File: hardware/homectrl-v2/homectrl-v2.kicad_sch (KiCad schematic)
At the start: 125 parts, among them J1 Barrel_Jack, J2 PUMP1_CONN, J3 PUMP2_CONN, J4 STEP_CONN, J5 USB_C_CONN, J6 SMS1_CONN, J7 ALS_CONN, J8 FSW1_CONN, Q1 AO3407A, Q2 2N7002, Q3 ZXMN3A01ZTA, Q4 ZXMN3A01ZTA, Q5 AO3400A, SW1 S3_RESET_SW, SW2 S3_BOOT_SW, U1 TPS5405DR, U2 MCP1826S, U3 DMP4065S-7, U4 ESP32-S3-WROOM-1, U5 TMC2209, U7 TPD4E001DRLR, U8 TPD2E001DRLR, U9 SI2347DS-T1-GE3

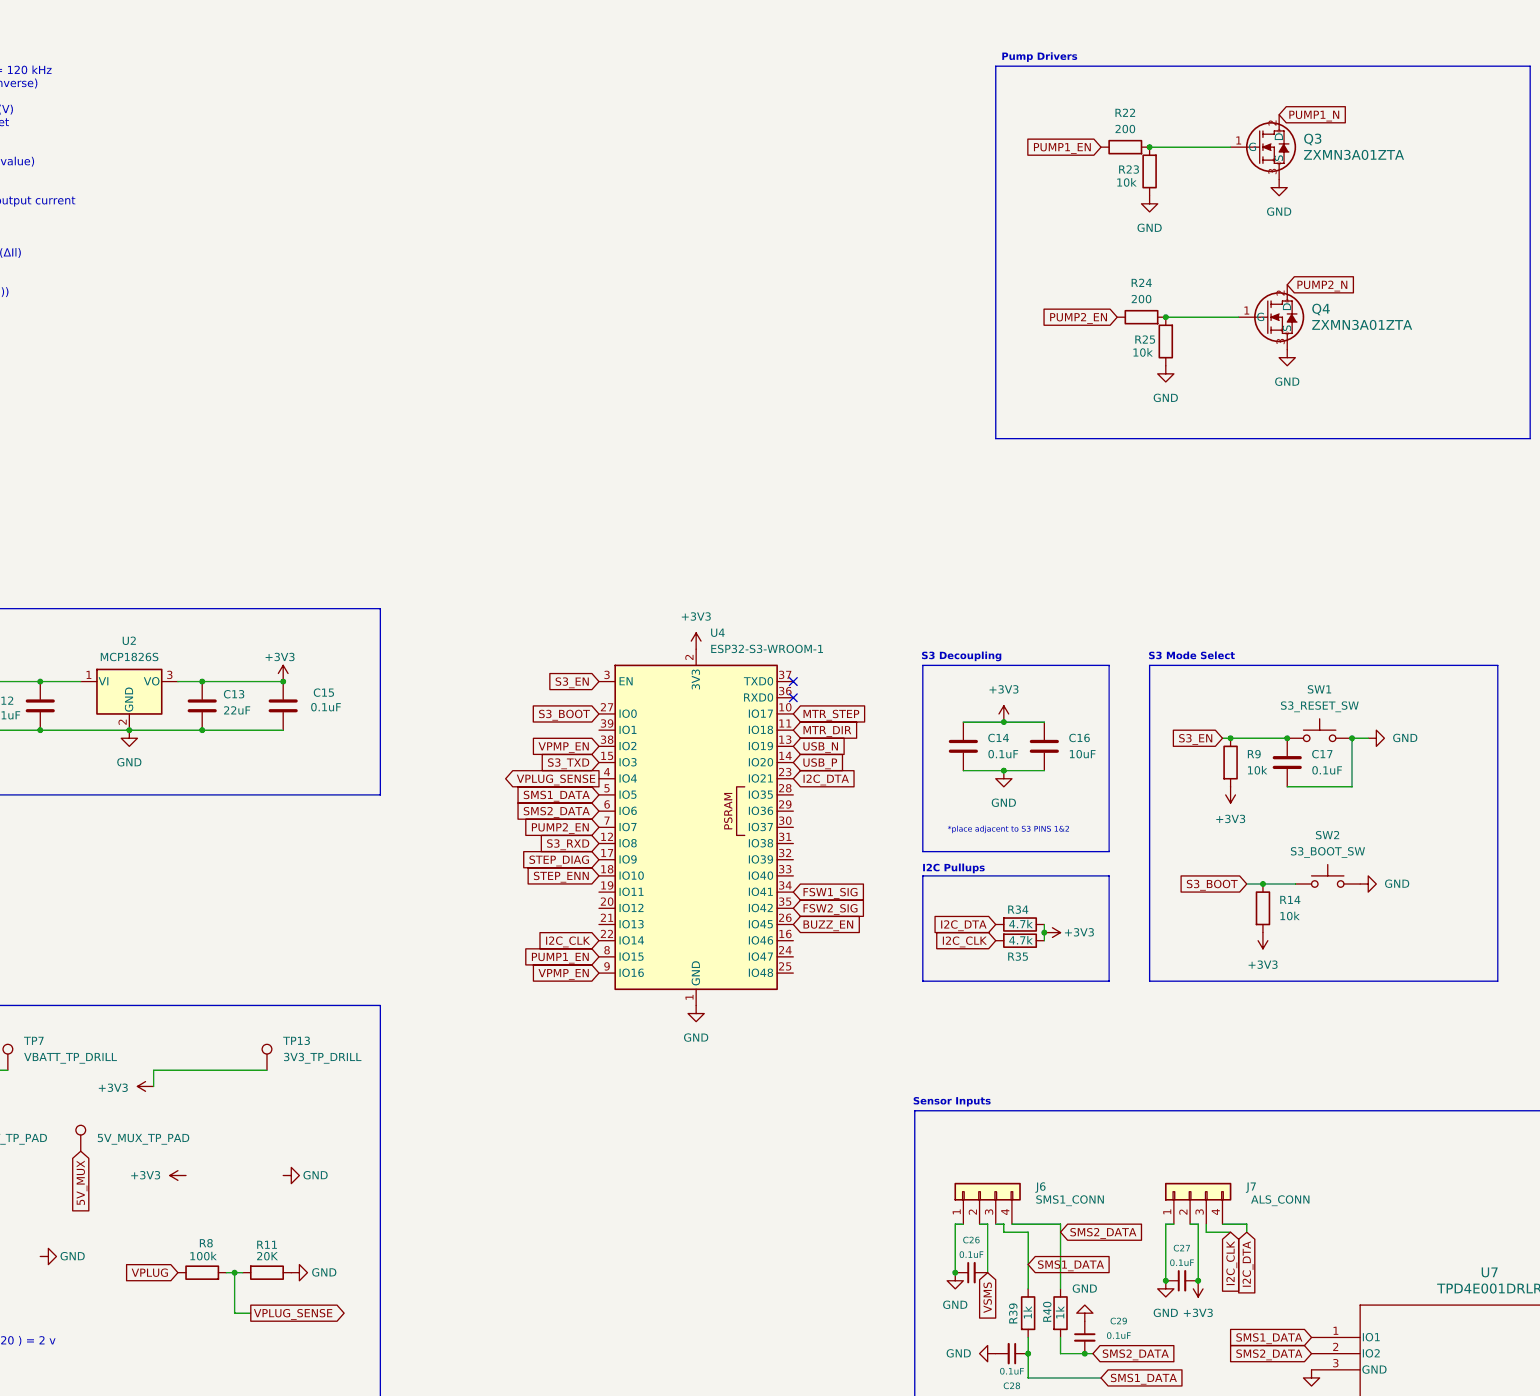
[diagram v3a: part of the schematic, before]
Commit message: finish component routing
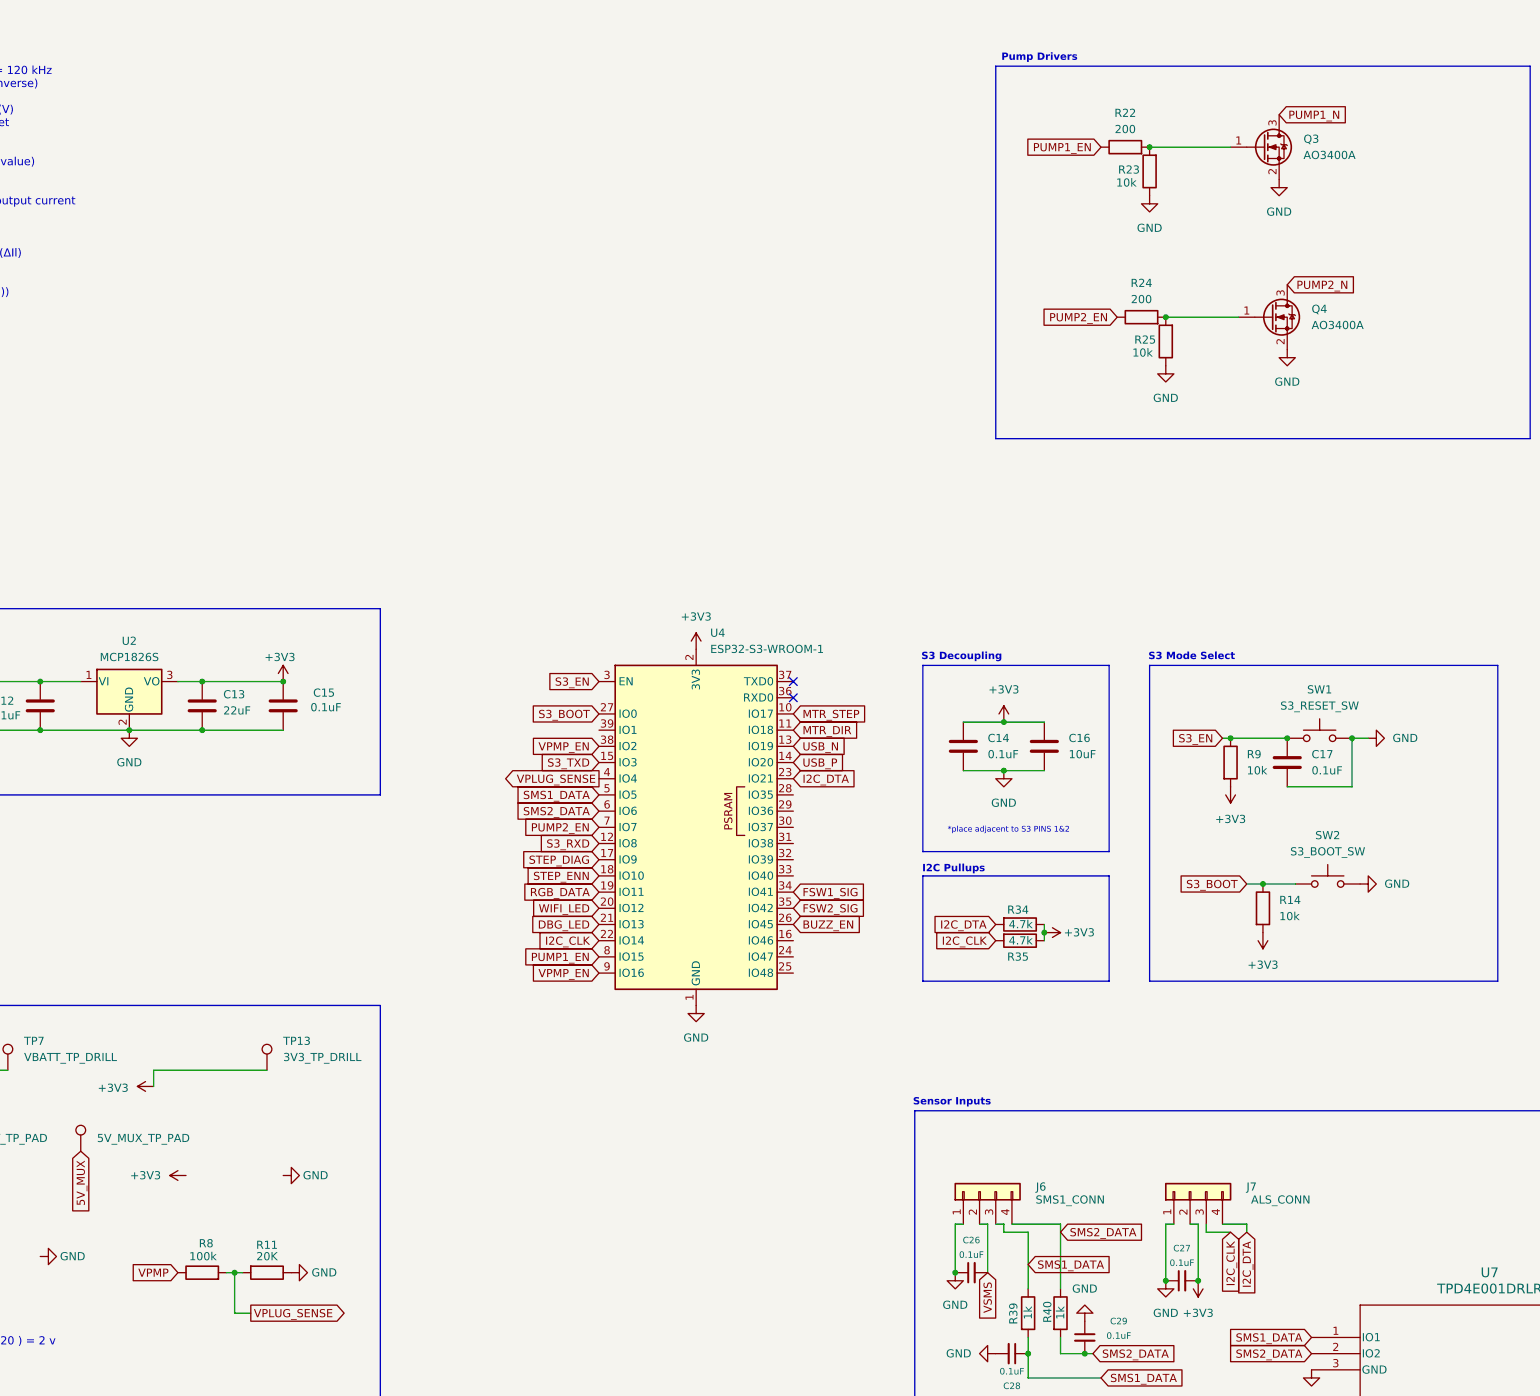
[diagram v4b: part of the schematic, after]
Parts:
- removed Q3, Q4: ZXMN3A01ZTA, Package_TO_SOT_SMD:SOT-89-3, symbol ZXMN3A01ZTA:ZXMN3A01ZTA
- added Q3, Q4: AO3400A, Package_TO_SOT_SMD:SOT-23, symbol Transistor_FET:AO3400A
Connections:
- net DBG_LED: now also U4.21 (IO13)
- net GND: now also Q3.2 (S), Q4.2 (S)
- net PUMP1_N: now also Q3.3 (D)
- net PUMP2_N: now also Q4.3 (D)
- net RGB_DATA: now also U4.19 (IO11)
- net VPLUG: no longer R8.1
- net VPMP: now also R8.1
- net WIFI_LED: now also U4.20 (IO12)
- net at R22.2, R23.2: now also Q3.1 (G)
- net at R24.2, R25.2: now also Q4.1 (G)
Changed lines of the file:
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@@
 		)
 	)
+	(global_label "WIFI_LED"
+		(shape input)
+		(at 259.08 226.06 180)
+		(fields_autoplaced yes)
+		(effects
+			(font
+				(size 1.27 1.27)
+			)
+			(justify right)
+		)
+		(property "Intersheetrefs" "${INTERSHEET_REFS}"
+			(at 247.9305 226.06 0)
+			(effects
+				(font
+					(size 1.27 1.27)
+				)
+				(justify right)
+				(hide yes)
+			)
+		)
+	)
 	(global_label "I2C_CLK"
 		(shape input)
@@
 		)
 	)
+	(global_label "VPMP"
+		(shape input)
+		(at 193.04 283.21 180)
+		(fields_autoplaced yes)
+		(effects
+			(font
+				(size 1.27 1.27)
+			)
+			(justify right)
+		)
+		(property "Intersheetrefs" "${INTERSHEET_REFS}"
+			(at 184.9748 283.21 0)
+			(effects
+				(font
+					(size 1.27 1.27)
+				)
+				(justify right)
+				(hide yes)
+			)
+		)
+	)
 	(global_label "VPLUG"
 		(shape input)
@@
 		)
 	)
-	(global_label "VPLUG"
-		(shape input)
-		(at 193.04 283.21 180)
-		(fields_autoplaced yes)
-		(effects
-			(font
-				(size 1.27 1.27)
-			)
-			(justify right)
-		)
-		(property "Intersheetrefs" "${INTERSHEET_REFS}"
-			(at 184.0676 283.21 0)
-			(effects
-				(font
-					(size 1.27 1.27)
-				)
-				(justify right)
-				(hide yes)
-			)
-		)
-	)
 	(global_label "FSW2_SIG"
 		(shape input)
@@
 		)
 	)
+	(global_label "DBG_LED"
+		(shape input)
+		(at 259.08 228.6 180)
+		(fields_autoplaced yes)
+		(effects
+			(font
+				(size 1.27 1.27)
+			)
+			(justify right)
+		)
+		(property "Intersheetrefs" "${INTERSHEET_REFS}"
+			(at 247.8701 228.6 0)
+			(effects
+				(font
+					(size 1.27 1.27)
+				)
+				(justify right)
+				(hide yes)
+			)
+		)
+	)
 	(global_label "VPMP"
 		(shape input)
@@
 		)
 	)
+	(global_label "RGB_DATA"
+		(shape input)
+		(at 259.08 223.52 180)
+		(fields_autoplaced yes)
+		(effects
+			(font
+				(size 1.27 1.27)
+			)
+			(justify right)
+		)
+		(property "Intersheetrefs" "${INTERSHEET_REFS}"
+			(at 246.9024 223.52 0)
+			(effects
+				(font
+					(size 1.27 1.27)
+				)
+				(justify right)
+				(hide yes)
+			)
+		)
+	)
 	(global_label "5V_MUX"
 		(shape input)
@@
 	)
 	(symbol
+		(lib_id "Transistor_FET:AO3400A")
+		(at 363.22 106.68 0)
+		(unit 1)
+		(exclude_from_sim no)
+		(in_bom yes)
+		(on_board yes)
+		(dnp no)
+		(fields_autoplaced yes)
+		(property "Reference" "Q3"
+			(at 369.57 105.4099 0)
+			(effects
+				(font
+					(size 1.27 1.27)
+				)
+				(justify left)
+			)
+		)
+		(property "Value" "AO3400A"
+			(at 369.57 107.9499 0)
+			(effects
+				(font
+					(size 1.27 1.27)
+				)
+				(justify left)
+			)
+		)
+		(property "Footprint" "Package_TO_SOT_SMD:SOT-23"
+			(at 368.3 108.585 0)
+			(effects
+				(font
+					(size 1.27 1.27)
+					(italic yes)
+				)
+				(justify left)
+				(hide yes)
+			)
+		)
+		(property "Datasheet" "http://www.aosmd.com/pdfs/datasheet/AO3400A.pdf"
+			(at 368.3 110.49 0)
+			(effects
+				(font
+					(size 1.27 1.27)
+				)
+				(justify left)
+				(hide yes)
+			)
+		)
+		(property "Description" "30V Vds, 5.7A Id, N-Channel MOSFET, SOT-23"
+			(at 363.22 106.68 0)
+			(effects
+				(font
+					(size 1.27 1.27)
+				)
+				(hide yes)
+			)
+		)
+		(pin "3"
+		)
+		(pin "2"
+		)
+		(pin "1"
+		)
+		(instances
+			(project ""
+				(path "/b68484f3-279c-4a19-afd1-e5b6591f7b52"
+					(reference "Q3")
+					(unit 1)
+				)
+			)
+		)
+	)
+	(symbol
 		(lib_id "Device:R")
 		(at 134.62 378.46 90)
@@
 	)
 	(symbol
+		(lib_id "Transistor_FET:AO3400A")
+		(at 364.49 133.35 0)
+		(unit 1)
+		(exclude_from_sim no)
+		(in_bom yes)
+		(on_board yes)
+		(dnp no)
+		(fields_autoplaced yes)
+		(property "Reference" "Q4"
+			(at 370.84 132.0799 0)
+			(effects
+				(font
+					(size 1.27 1.27)
+				)
+				(justify left)
+			)
+		)
+		(property "Value" "AO3400A"
+			(at 370.84 134.6199 0)
+			(effects
+				(font
+					(size 1.27 1.27)
+				)
+				(justify left)
+			)
+		)
+		(property "Footprint" "Package_TO_SOT_SMD:SOT-23"
+			(at 369.57 135.255 0)
+			(effects
+				(font
+					(size 1.27 1.27)
+					(italic yes)
+				)
+				(justify left)
+				(hide yes)
+			)
+		)
+		(property "Datasheet" "http://www.aosmd.com/pdfs/datasheet/AO3400A.pdf"
+			(at 369.57 137.16 0)
+			(effects
+				(font
+					(size 1.27 1.27)
+				)
+				(justify left)
+				(hide yes)
+			)
+		)
+		(property "Description" "30V Vds, 5.7A Id, N-Channel MOSFET, SOT-23"
+			(at 364.49 133.35 0)
+			(effects
+				(font
+					(size 1.27 1.27)
+				)
+				(hide yes)
+			)
+		)
+		(pin "3"
+		)
+		(pin "2"
+		)
+		(pin "1"
+		)
+		(instances
+			(project "homectrl-v2"
+				(path "/b68484f3-279c-4a19-afd1-e5b6591f7b52"
+					(reference "Q4")
+					(unit 1)
+				)
+			)
+		)
+	)
+	(symbol
 		(lib_id "power:GND")
 		(at 422.91 359.41 90)
@@
 	)
 	(symbol
-		(lib_id "ZXMN3A01ZTA:ZXMN3A01ZTA")
-		(at 358.14 106.68 0)
-		(unit 1)
-		(exclude_from_sim no)
-		(in_bom yes)
-		(on_board yes)
-		(dnp no)
-		(fields_autoplaced yes)
-		(property "Reference" "Q3"
-			(at 369.57 105.4099 0)
-			(effects
-				(font
-					(size 1.524 1.524)
-				)
-				(justify left)
-			)
-		)
-		(property "Value" "ZXMN3A01ZTA"
-			(at 369.57 107.9499 0)
-			(effects
-				(font
-					(size 1.524 1.524)
-				)
-				(justify left)
-			)
-		)
-		(property "Footprint" "Package_TO_SOT_SMD:SOT-89-3"
-			(at 358.14 106.68 0)
-			(effects
-				(font
-					(size 1.27 1.27)
-					(italic yes)
-				)
-				(hide yes)
-			)
-		)
-		(property "Datasheet" "ZXMN3A01ZTA"
-			(at 358.14 106.68 0)
-			(effects
-				(font
-					(size 1.27 1.27)
-					(italic yes)
-				)
-				(hide yes)
-			)
-		)
-		(property "Description" ""
-			(at 358.14 106.68 0)
-			(effects
-				(font
-					(size 1.27 1.27)
-				)
-				(hide yes)
-			)
-		)
-		(pin "2"
-		)
-		(pin "1"
-		)
-		(pin "3"
-		)
-		(instances
-			(project ""
-				(path "/b68484f3-279c-4a19-afd1-e5b6591f7b52"
-					(reference "Q3")
-					(unit 1)
-				)
-			)
-		)
-	)
-	(symbol
 		(lib_id "Device:R")
 		(at 50.8 100.33 180)
@@
 					(unit 1)
 				)
-			)
-		)
-	)
-	(symbol
-		(lib_id "ZXMN3A01ZTA:ZXMN3A01ZTA")
-		(at 359.41 133.35 0)
-		(unit 1)
-		(exclude_from_sim no)
-		(in_bom yes)
-		(on_board yes)
-		(dnp no)
-		(fields_autoplaced yes)
-		(property "Reference" "Q4"
-			(at 370.84 132.0799 0)
-			(effects
-				(font
-					(size 1.524 1.524)
-				)
-				(justify left)
-			)
-		)
-		(property "Value" "ZXMN3A01ZTA"
-			(at 370.84 134.6199 0)
-			(effects
-				(font
-					(size 1.524 1.524)
-				)
-				(justify left)
-			)
-		)
-		(property "Footprint" "Package_TO_SOT_SMD:SOT-89-3"
-			(at 359.41 133.35 0)
-			(effects
-				(font
-					(size 1.27 1.27)
-					(italic yes)
-				)
-				(hide yes)
-			)
-		)
-		(property "Datasheet" "ZXMN3A01ZTA"
-			(at 359.41 133.35 0)
-			(effects
-				(font
-					(size 1.27 1.27)
-					(italic yes)
-				)
-				(hide yes)
-			)
-		)
-		(property "Description" ""
-			(at 359.41 133.35 0)
-			(effects
-				(font
-					(size 1.27 1.27)
-				)
-				(hide yes)
-			)
-		)
-		(pin "1"
-		)
-		(pin "3"
-		)
-		(pin "2"
-		)
-		(instances
-			(project ""
-				(path "/b68484f3-279c-4a19-afd1-e5b6591f7b52"
-					(reference "Q4")
-					(unit 1)
-				)

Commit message: logic power routing
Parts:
- removed BZ1: SMT-0540-S-R, SMT-0540-S-R:XDCR_SMT-0540-S-R, symbol SMT-0540-S-R:SMT-0540-S-R
- removed C21: 0.1uF, Capacitor_SMD:C_0402_1005Metric, symbol Device:C
- removed D13: 1N4148W, Diode_SMD:D_SOD-123, symbol Device:D
- removed Q5: AO3400A, Package_TO_SOT_SMD:SOT-23, symbol Transistor_FET:2N7002
- removed R16: 200, Resistor_SMD:R_0402_1005Metric, symbol Device:R
- removed R19: 10k, Resistor_SMD:R_0402_1005Metric, symbol Device:R
- removed TP13: 3V3_TP_DRILL, TestPoint:TestPoint_THTPad_D1.0mm_Drill0.5mm, symbol Connector:TestPoint
- removed TP7: VBATT_TP_DRILL, TestPoint:TestPoint_THTPad_D1.0mm_Drill0.5mm, symbol Connector:TestPoint
- added D7: PLUG_LED, LED_SMD:LED_0603_1608Metric, symbol Device:LED
- added R12: 1K, Resistor_SMD:R_0402_1005Metric, symbol Device:R
- J8: footprint JST_XH_B3B-XH-AM_1x03_P2.50mm_Vertical -> Connector_JST:JST_XH_B3B-XH-A_1x03_P2.50mm_Vertical
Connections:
- net FSW1_SIG: no longer J8.1 (Pin_1), R26.2, R27.2, U8.3 (IO1)
- net FSW2_SIG: no longer J8.2 (Pin_2), R28.2, R32.2, U8.5 (IO2)
- net GND: now also D7.1 (K)
- net SMS1_DATA: no longer J6.3 (Pin_3), R39.1, U7.1 (IO1)
- net SMS2_DATA: no longer J6.4 (Pin_4), R40.1, U7.2 (IO2)
- net VPLUG: now also R12.2
- net BUZZ_EN: no longer names the net of U4.26 (IO45)
- net VPLUG_SENSE renamed VPMP_SENSE
- new net: D7.2 (A), R12.1
- new net: J6.4 (Pin_4), R40.1, U7.1 (IO1)
- new net: J8.2 (Pin_2), R28.2, R32.2, U8.5 (IO2)
- new net: J6.3 (Pin_3), R39.1, U7.2 (IO2)
- new net: J8.1 (Pin_1), R26.2, R27.2, U8.3 (IO1)
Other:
- note removed: "Buzzer Driver"
- note removed: "flyback diode to protect against inductive spikes"
- moved on the sheet: C20, D11, D12, D14, J5, R17, R18, R20, R21

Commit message: wrapping up layout & routing
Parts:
- added BZ1: CMT-0525-75-SMT-TR, CMT_0525_75_SMT_TR:XDCR_CMT-0525-75-SMT-TR, symbol CMT-0525-75-SMT-TR:CMT-0525-75-SMT-TR
- added C21: 0.1uF, Capacitor_SMD:C_0402_1005Metric, symbol Device:C_Small
- added D10: ON_LED, LED_SMD:LED_0603_1608Metric, symbol Device:LED
- added D13: BAT54J, Diode_SMD:D_SOD-323F, symbol Diode:BAT54J
- added D8: 3V3_LED, LED_SMD:LED_0603_1608Metric, symbol Device:LED
- added Q5: AO3400A, Package_TO_SOT_SMD:SOT-23, symbol Transistor_FET:AO3400A
- added R13, R15: 330, Resistor_SMD:R_0402_1005Metric, symbol Device:R
- added R16: 200, Resistor_SMD:R_0402_1005Metric, symbol Device:R
- added R19: 10k, Resistor_SMD:R_0402_1005Metric, symbol Device:R
- added TP2: 3V3_TP_PAD, TestPoint:TestPoint_Pad_1.5x1.5mm, symbol Connector:TestPoint
- added TP5: VPLUG_TP_PAD, TestPoint_Pad_D1.0mm, symbol Connector:TestPoint
- D2: footprint Diode_SMD:D_0603_1608Metric -> LED_SMD:LED_0603_1608Metric
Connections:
- net +3V3: now also BZ1.P, C21.1, D13.1 (K), R13.2, R15.2, TP2.1
- net GND: now also D10.1 (K), D8.1 (K), Q5.2 (S), R19.1
- net VPLUG: no longer R12.2
- net VPMP_EN: no longer R36.1, U4.38 (IO2)
- net BUZZ_EN: now reaches U4.24 (IO47)
- net BUZZ_EN: now also R16.1
- new net: R12.2, TP5.1
- new net: BZ1.N, C21.2, D13.2 (A), Q5.3 (D)
- new net: Q5.1 (G), R16.2, R19.2
- new net: D10.2 (A), R15.1
- new net: D8.2 (A), R13.1
- new net VSMS_EN: R36.1, U4.38 (IO2)
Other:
- note added: "Buzzer Driver"
- moved on the sheet: D7, R12, TP4

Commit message: reviewed
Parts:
- added D15: VPMP_LED, LED_SMD:LED_0603_1608Metric, symbol Device:LED
- added R37: 1.8K, Resistor_SMD:R_0402_1005Metric, symbol Device:R
- D11: value WIFI_LED -> DBG_LED; LCSC C72041 -> C72038
- D12: value DBG_LED -> WIFI_LED; LCSC C72038 -> C72041
- D13: LCSC (none) -> C86299
- D7, D8: LCSC C2297 -> C12065
- Q3, Q4, Q5: LCSC (none) -> C20917
- R10: value 680 -> 470; LCSC C23228 -> C25167
- R12: value 1K -> 1.8K
- R13, R15: value 330 -> 150; LCSC C23228 -> C25082
- R16: value 200 -> 150; LCSC (none) -> C25082
- R17: value 330 -> 150; LCSC C25104 -> C25082
- R18: LCSC C72038 -> C25082
- R19: LCSC (none) -> C25744
- R20, R21: LCSC C23186 -> C25905
- R22, R24, R36, R7: value 200 -> 150; LCSC C8218 -> C25082
- R29, R30: footprint Resistor_SMD:R_0402_1005Metric -> Resistor_SMD:R_0603_1608Metric; LCSC (none) -> C247140
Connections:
- net BUZZ_EN: now also R16.2; no longer R16.1
- net DBG_LED: now also R17.2; no longer R17.1
- net GND: now also D15.1 (K)
- net PUMP1_EN: now also R22.2; no longer R22.1
- net PUMP2_EN: now also R24.2; no longer R24.1
- net VPMP: now also R37.2
- net WIFI_LED: now also R18.2; no longer R18.1
- net at J6.4 (Pin_4), R40.1: now also U7.2 (IO2); no longer U7.1 (IO1)
- net at Q3.1 (G), R23.2: now also R22.1; no longer R22.2
- net at J6.3 (Pin_3), R39.1: now also U7.1 (IO1); no longer U7.2 (IO2)
- net at R12.2, TP5.1: now also C1.1, D3.1 (K), FB1.1, U9.2
- net at D11.2 (A): now also R17.1; no longer R17.2
- net at Q4.1 (G), R25.2: now also R24.1; no longer R24.2
- net at D12.2 (A): now also R18.1; no longer R18.2
- net at Q5.1 (G), R19.2: now also R16.1; no longer R16.2
- new net: D15.2 (A), R37.1
- no-connect marks 8 -> 18

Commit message: added part numbers
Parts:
- BZ1, C1, C34, D1, D14, D5, D9, F1, FB1, J1, J2, J3, J4, J6, J7, J8: now not fitted
- C10, C12, C15, C7, C9: LCSC C14663 -> C77020
- C11: LCSC C15850 -> (none)
- C14, C17, C21, C24, C26, C27, C28, C29, C30, C31, C32, C35, C36, C37, C39, C41, C43, C5: LCSC (none) -> C77020
- C18, C19: LCSC (none) -> C14663
- C2, C3: LCSC (none) -> C15850
- C20: LCSC C1581 -> C77020
- C22, C23: LCSC (none) -> C913517
- C38: LCSC (none) -> C1532
- C4: LCSC (none) -> C15195
- C40: LCSC (none) -> C72203
- C8: LCSC (none) -> C26404
- D3: LCSC (none) -> C2856864
- D4: LCSC (none) -> C5380710
- Q1: LCSC (none) -> C15155
- R10: LCSC C25167 -> C174152
- R11: LCSC (none) -> C22356231
- R12, R37: LCSC C23228 -> C174229
- R14, R4, R9: LCSC (none) -> C25744
- R2: LCSC (none) -> C1996
- R23, R25, R26, R28, R33, R5, R6: LCSC C25804 -> C25744
- R27, R32, R39, R40: LCSC C25804 -> C11702
- R3: LCSC (none) -> C166559
- R31: LCSC (none) -> C11702
- R8: LCSC C25803 -> C25741
- SW1, SW2: LCSC (none) -> C561521
- U2: LCSC (none) -> C638624
- U4: LCSC (none) -> C2913199
- U5: LCSC (none) -> C2150710
- U7: LCSC (none) -> C527516
- U8: LCSC (none) -> C150526
- U9: LCSC (none) -> C145002
